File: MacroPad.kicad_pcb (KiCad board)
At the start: 2 copper layers, 111.6 x 82.3 mm, 42 parts, among them J1 Conn_01x04_Pin, SW1 SW_Push, SW10 SW_Push, SW11 SW_Push, SW12 SW_Push, SW13 RotaryEncoder_Switch, SW14 RotaryEncoder_Switch, SW2 SW_Push, SW3 SW_Push, SW4 SW_Push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

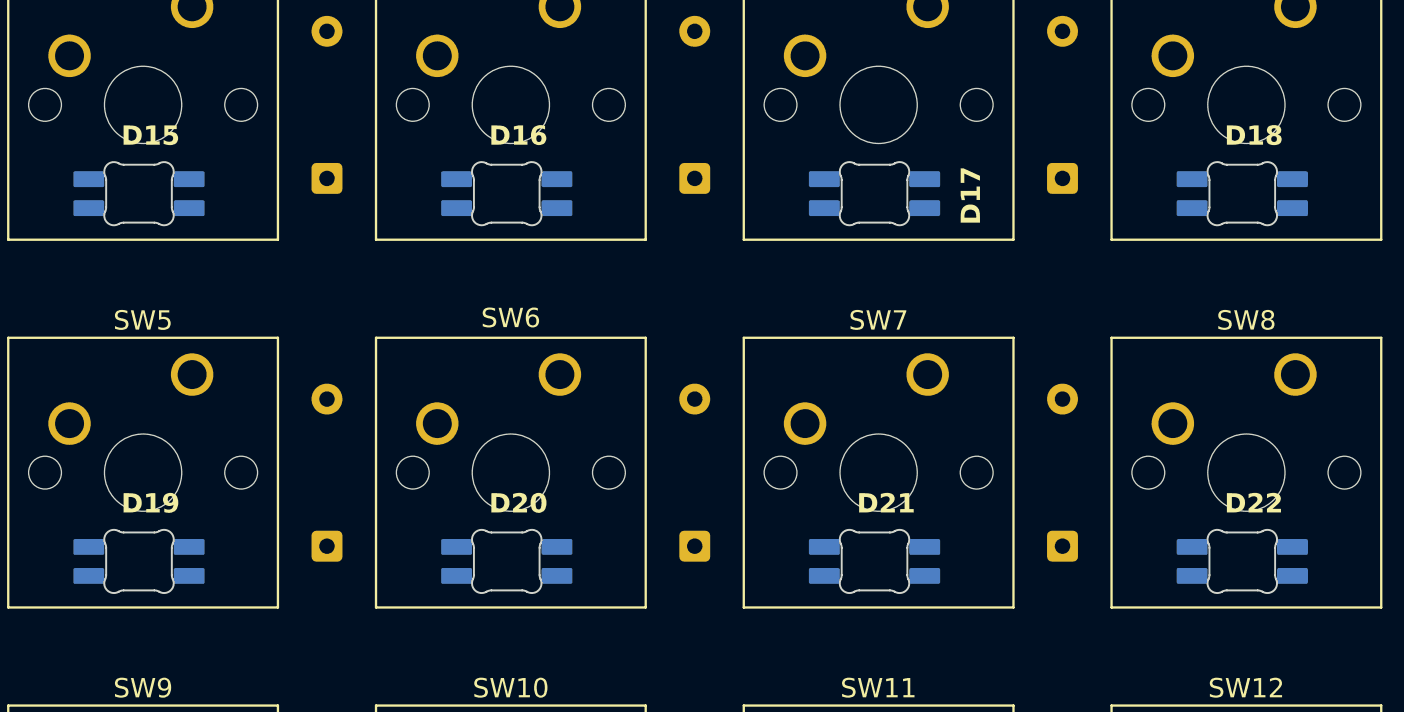
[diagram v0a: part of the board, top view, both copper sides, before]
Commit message: feat: switched switches
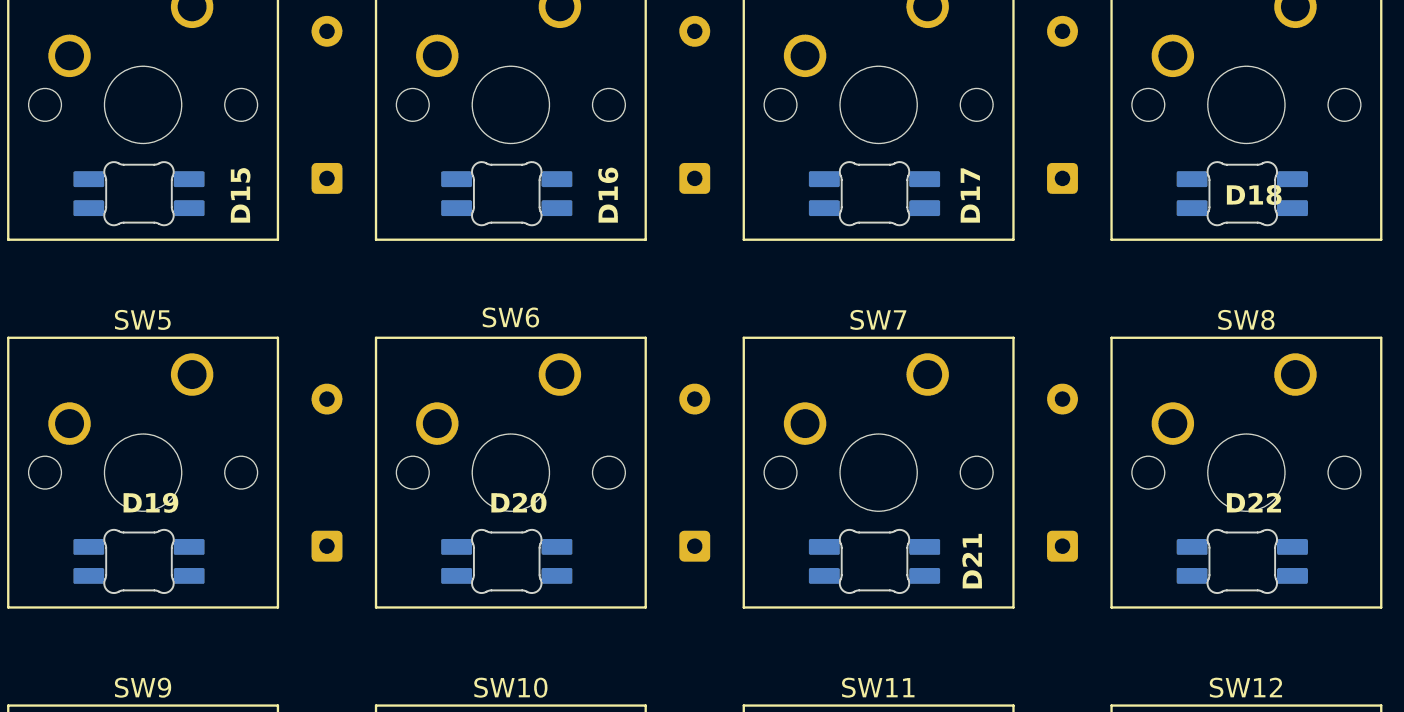
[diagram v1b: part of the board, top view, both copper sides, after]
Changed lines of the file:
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@@
 		(tags "cherry MX SK6812 Mini-E rearmount rear mount led rgb backlight")
 		(property "Reference" "D16"
-			(at 0.6 -3.1 0)
+			(at 5.292501 0 90)
 			(layer "F.SilkS")
 			(effects
@@
 		(tags "cherry MX SK6812 Mini-E rearmount rear mount led rgb backlight")
 		(property "Reference" "D18"
-			(at 0.6 -3.1 0)
+			(at 0.6 0 0)
 			(layer "F.SilkS")
 			(effects
@@
 		(tags "cherry MX SK6812 Mini-E rearmount rear mount led rgb backlight")
 		(property "Reference" "D15"
-			(at 0.6 -3.1 0)
+			(at 5.292501 0 90)
 			(layer "F.SilkS")
 			(effects
@@
 		)
 		(group ""
-			(members "09d9c330-ecd0-4cf5-89e1-1cb806b424a2" "250bae45-1c97-4358-8a60-486c77ef44fa"
-				"2e01f201-9932-4cbc-a2b4-000c127eed1b" "2e54bba2-ecc7-450d-b97f-8bab4bf9cb57"
-				"32814cc3-ef5d-437f-801f-61bf98d32a59" "3542fcaf-ad4e-467f-9c3d-002519e002c7"
-				"358014bd-7b15-4b7f-b0e1-6c1eddcb03df" "3e85f184-dbde-4694-8cc2-57e22249d30a"
-				"46d54e61-7f71-4004-a564-659e86bd79a6" "4d6e28b2-8a82-493a-b684-9271a7b2452e"
-				"501534d5-724a-45af-b9f0-9079ed81aa62" "5034492f-c4b7-4322-8867-4f45332e1c39"
-				"55aeaa43-bea0-400a-a70b-e0472a4f458f" "5a02b556-12d8-4989-be5d-d536a6437e56"
-				"6ab7f9a8-1f91-4d44-9753-b51534d8d8f4" "6d86b246-2b53-4f61-9c86-f7111de0457f"
-				"75d4e6c9-b352-48fa-a5cb-75e2915dd4c3" "7ea0aa41-bb6c-4838-a7bb-ad1cc9b0fdfe"
-				"8d22b730-c018-4328-8404-b2145ae50457" "906edeae-4b98-4910-9a5a-c1d945368e82"
-				"90ebe5e5-bf42-40c0-b3d7-a98e35e53ba3" "92d3a136-8f37-4cee-b70f-de84c823bfbf"
-				"947943cf-3d59-46b2-987a-6979669d9f25" "9597d64c-06b1-42b9-9697-4e5d7491b230"
-				"9a700cb4-6201-41f4-a3bb-845ce9ea87f5" "9a78f9e5-744e-41c0-82ce-08c24619f8c4"
-				"9b5dc3c4-ec41-49ef-954a-99a3045b8e03" "9e6f9f66-5cbe-4461-95dc-5723ff38c3c6"
-				"9f4daaee-5f3d-4d2c-8a6e-5f8c2fce7eb5" "a8fe86c1-029a-42d2-9fd9-e542c352877e"
-				"a9c6a32b-da02-4fac-beb3-94eae5d9e131" "aa4f680e-f05e-4b5a-a456-715b0d4001c9"
-				"aa88852c-55ac-4298-a7c7-316ede0a45c9" "b4a9b873-53e0-413f-81a4-1fee5c6b5185"
-				"c29a122d-b751-4b60-b5e0-3c247505d195" "c56f8a3c-36fb-49c1-8919-16a7cd2785b0"
-				"d19b58ff-8ee2-4cd7-b5d6-69b9b12989f9" "e2ba5baf-3eff-4689-98f3-51c7eff9457f"
-				"e3016d8c-054c-4e0f-8a03-737b9f193e7d" "e32a382e-97ab-4c1b-978a-c90f82d39715"
-				"e815d31f-ed88-47c1-8349-eac2842548a5" "ea17a197-c345-4ec1-b1af-02c28521a814"
-				"ee744702-1105-4246-9a7c-e80697756f15" "ef099137-af15-423f-aaef-de424383caae"
-				"f5b685c1-7f78-46aa-b14d-ec7269964336" "fb14cc32-e23a-4a3a-a645-bdc3ce0c2a3c"
-				"fbeb4153-a81c-4e40-bd3b-a176a439c8da" "fff28b0f-de4e-4e38-ba7c-a24ccf695cf8"
-			)
-		)
-		(group ""
-			(members "061158ff-03d0-42e0-bdcb-69caadfd68d8" "084a3624-a4b8-4d11-89c1-dffbd1a2d27a"
-				"0e498a36-7944-4a8d-9b73-08c20f32402e" "1210d1b9-4e94-4a9f-8af5-f90286309a55"
-				"14e8c5c1-1b32-45a5-bba2-bc51e3b03aff" "166b48ad-069a-45be-aa50-45eb2e5e4ecb"
-				"4ff4b023-7b39-4901-b95d-b2cbd2305812" "58d544c9-b25f-4e46-ba22-b90f72a108bb"
-				"5bba9753-d765-430d-8060-259791c686a0" "662c3d8f-80e3-40a4-9ee5-2052b8853467"
-				"6e8a4f9c-dc7d-4911-934a-e7ef929f23bc" "759188b4-9434-47da-84b5-da10fc2fdd50"
-				"7a5a5cae-3613-4cec-849d-7cc3ded252de" "7cab4fc5-1952-4926-b7ca-e3d956245fa0"
-				"7ef5dcf8-d4ed-495a-bf8e-299445a17f8a" "8f1f9102-266d-4737-aff6-5ea8320629d7"
-				"98897d81-897f-4147-a157-240bf28e5d67" "9cd43913-5e1c-49c1-a2e2-2880e7fe4e70"
-				"9cd7ea6d-7d9d-4a8d-8efc-b619073b824f" "9f383c72-edaf-44dd-9810-24d9ac8d7c6c"
-				"a4244ca3-faf4-4ced-bffa-8034747dc680" "a569df4b-07a7-4970-ba91-d2a8037fbc20"
-				"aa57b36b-cbb0-4894-9c24-bbc69f9e5bd4" "afd1c8ee-05b0-4483-acd9-582cd8b80be7"
-				"b681146b-c265-464a-a32a-16bad65ba085" "be486314-a5f8-45fe-a6f8-0e7cef5d0f4e"
-				"d7474648-1a69-4a97-ae2f-b6c65880bad1" "dcbf3872-4671-4f97-b600-23d6b0046d59"
-			)
-		)
-		(group ""
 			(members "0485025b-c323-49ba-84c2-b5c503d9fbfd" "04be1a19-7e8b-421e-8ac8-41789944170a"
 				"09d9c330-ecd0-4cf5-89e1-1cb806b424a2" "1127f61d-185d-4932-869f-fb6172a3f5ec"
@@
 		)
 		(group ""
+			(members "061158ff-03d0-42e0-bdcb-69caadfd68d8" "084a3624-a4b8-4d11-89c1-dffbd1a2d27a"
+				"0e498a36-7944-4a8d-9b73-08c20f32402e" "1210d1b9-4e94-4a9f-8af5-f90286309a55"
+				"14e8c5c1-1b32-45a5-bba2-bc51e3b03aff" "166b48ad-069a-45be-aa50-45eb2e5e4ecb"
+				"4ff4b023-7b39-4901-b95d-b2cbd2305812" "58d544c9-b25f-4e46-ba22-b90f72a108bb"
+				"5bba9753-d765-430d-8060-259791c686a0" "662c3d8f-80e3-40a4-9ee5-2052b8853467"
+				"6e8a4f9c-dc7d-4911-934a-e7ef929f23bc" "759188b4-9434-47da-84b5-da10fc2fdd50"
+				"7a5a5cae-3613-4cec-849d-7cc3ded252de" "7cab4fc5-1952-4926-b7ca-e3d956245fa0"
+				"7ef5dcf8-d4ed-495a-bf8e-299445a17f8a" "8f1f9102-266d-4737-aff6-5ea8320629d7"
+				"98897d81-897f-4147-a157-240bf28e5d67" "9cd43913-5e1c-49c1-a2e2-2880e7fe4e70"
+				"9cd7ea6d-7d9d-4a8d-8efc-b619073b824f" "9f383c72-edaf-44dd-9810-24d9ac8d7c6c"
+				"a4244ca3-faf4-4ced-bffa-8034747dc680" "a569df4b-07a7-4970-ba91-d2a8037fbc20"
+				"aa57b36b-cbb0-4894-9c24-bbc69f9e5bd4" "afd1c8ee-05b0-4483-acd9-582cd8b80be7"
+				"b681146b-c265-464a-a32a-16bad65ba085" "be486314-a5f8-45fe-a6f8-0e7cef5d0f4e"
+				"d7474648-1a69-4a97-ae2f-b6c65880bad1" "dcbf3872-4671-4f97-b600-23d6b0046d59"
+			)
+		)
+		(group ""
 			(members "0db2cdef-5d52-44a4-b6bb-015cbc59f342" "10360150-7f7c-4eb3-8b60-53bf5bf6a304"
 				"1c2c1d03-fb6e-491e-9aeb-248e89d53223" "2c1abc88-3eab-40a2-a10d-013b9bade79a"
@@
 		)
 		(group ""
+			(members "358014bd-7b15-4b7f-b0e1-6c1eddcb03df" "4d6e28b2-8a82-493a-b684-9271a7b2452e"
+				"5034492f-c4b7-4322-8867-4f45332e1c39" "75d4e6c9-b352-48fa-a5cb-75e2915dd4c3"
+				"8d22b730-c018-4328-8404-b2145ae50457" "aa88852c-55ac-4298-a7c7-316ede0a45c9"
+				"e815d31f-ed88-47c1-8349-eac2842548a5" "ea17a197-c345-4ec1-b1af-02c28521a814"
+			)
+		)
+		(group ""
 			(members "6b6fc1f7-29f9-4ac2-8893-02d16f6a9456" "9a723a52-c85c-45d1-9a2b-789e5c34bd6b")
 		)
@@
 		(tags "cherry MX SK6812 Mini-E rearmount rear mount led rgb backlight")
 		(property "Reference" "D21"
-			(at 0.6 -3.1 0)
+			(at 5.102501 -0.102842 90)
 			(layer "F.SilkS")
 			(effects

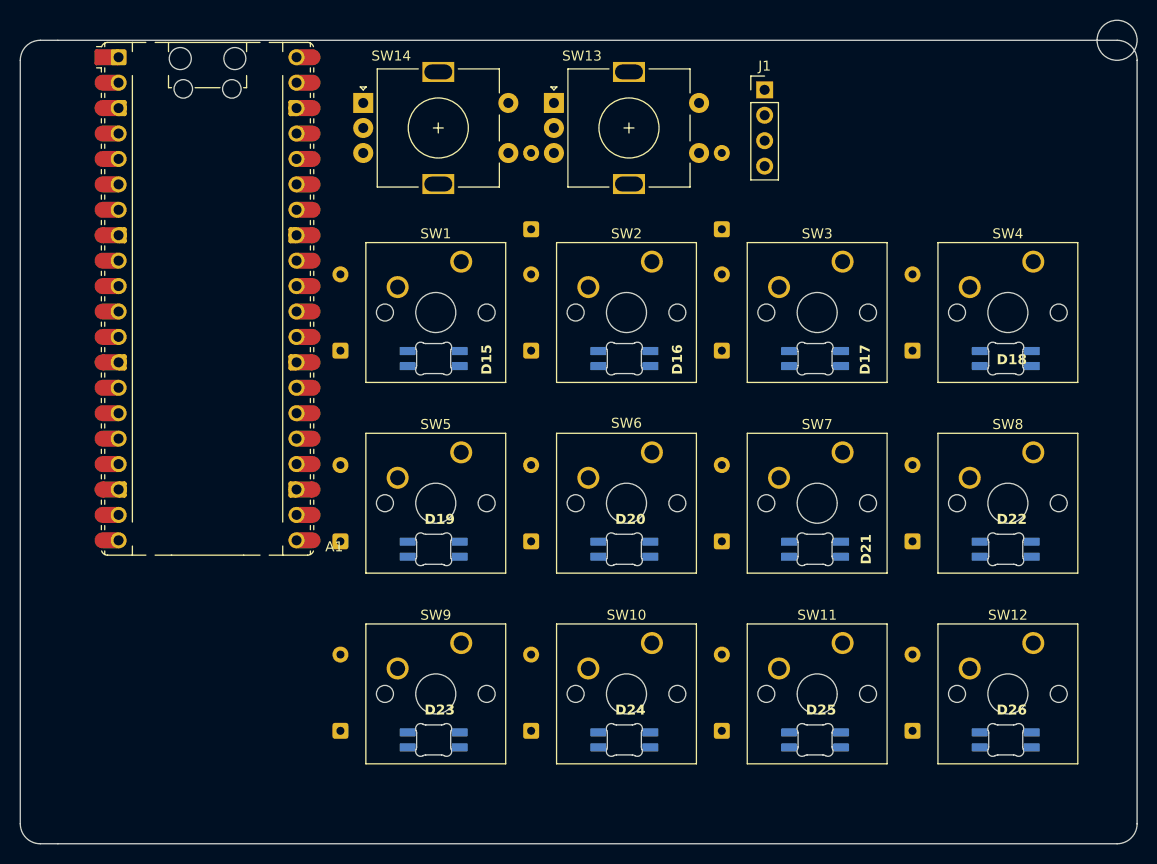
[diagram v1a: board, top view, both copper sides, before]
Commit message: feat: change blueprints
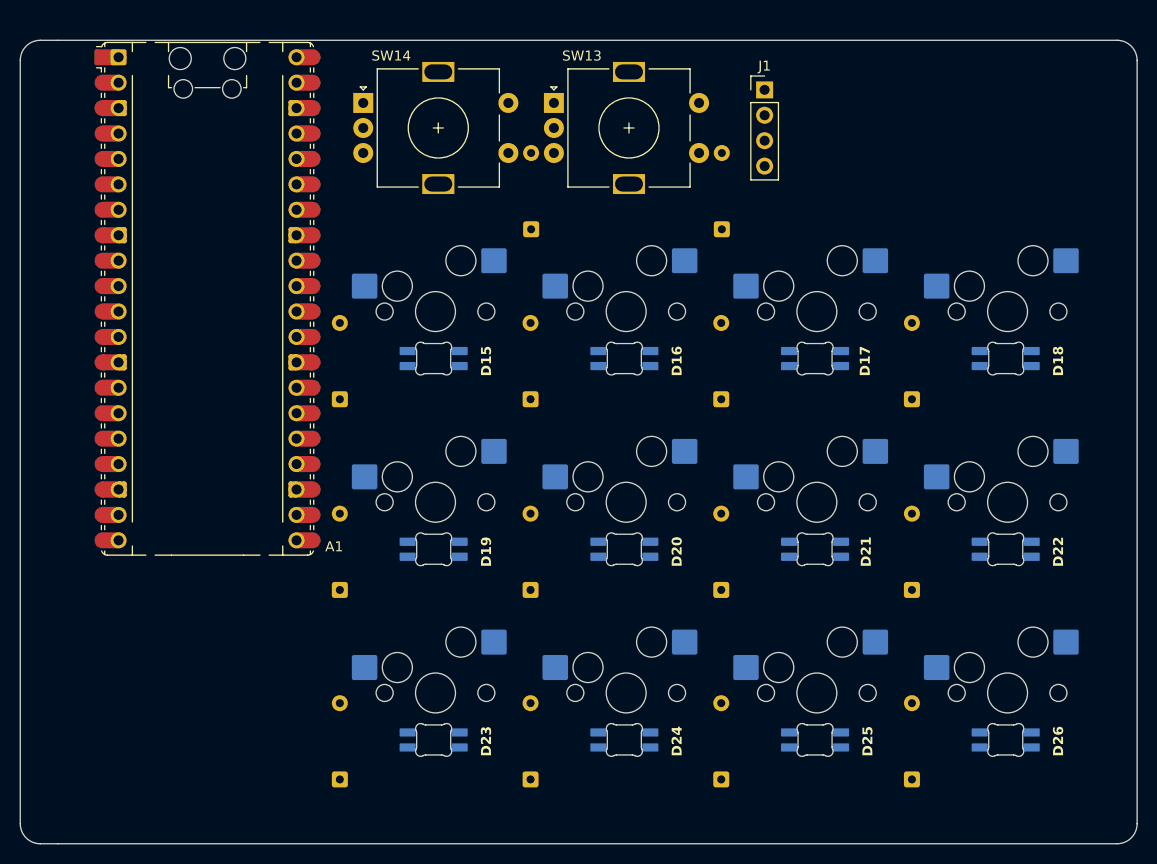
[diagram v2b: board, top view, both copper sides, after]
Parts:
- SW1, SW10, SW11, SW12, SW2, SW3, SW4, SW5, SW6, SW7, SW8, SW9: footprint Button_Switch_Keyboard:SW_Cherry_MX_1.00u_PCB -> Switch_MX_Hotswap:MX-Hotswap-1U; moved to B.Cu
- moved SW1 5.61 mm to (136.5, 80.9), turned to 180 degrees
- moved SW5 5.61 mm to (136.5, 100.0), turned to 180 degrees
- moved SW9 5.61 mm to (136.5, 119.0), turned to 180 degrees
- moved SW10 5.61 mm to (155.5, 119.0), turned to 180 degrees
- moved SW11 5.61 mm to (174.6, 119.0), turned to 180 degrees
- moved SW12 5.61 mm to (193.6, 119.0), turned to 180 degrees
- moved SW2 5.61 mm to (155.5, 80.9), turned to 180 degrees
- moved SW3 5.61 mm to (174.6, 80.9), turned to 180 degrees
- moved SW4 5.61 mm to (193.6, 80.9), turned to 180 degrees
- moved SW6 5.61 mm to (155.5, 100.0), turned to 180 degrees
- moved SW7 5.61 mm to (174.6, 100.0), turned to 180 degrees
- moved SW8 5.61 mm to (193.6, 100.0), turned to 180 degrees
- moved D1 4.86 mm to (126.9, 89.7)
- moved D10 4.86 mm to (146.0, 127.7)
- moved D11 4.86 mm to (165.0, 127.7)
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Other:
- board size 111.6 x 82.3 mm -> 111.6 x 80.3 mm
